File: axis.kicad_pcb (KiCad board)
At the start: 4 copper layers, 66 x 18 mm, 48 parts, among them J101 CORTEX-DEBUG, J102 JAE_DX07S016JA1R1500, SW101 SW_Push, SW102 SW_Push, U101 BHI160, U102 ATSAMD51G, U103 BMM150, U104 AP2112K-3.3, Y101 32.768kHz

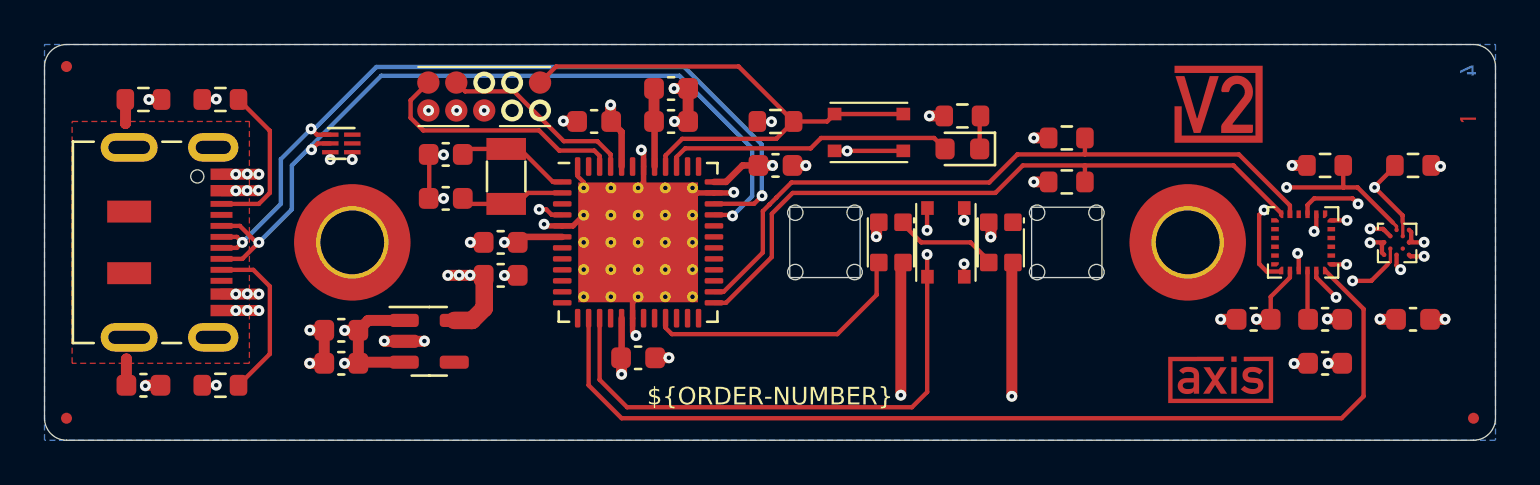
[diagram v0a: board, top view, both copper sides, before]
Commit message: Update to KiCat 7.0
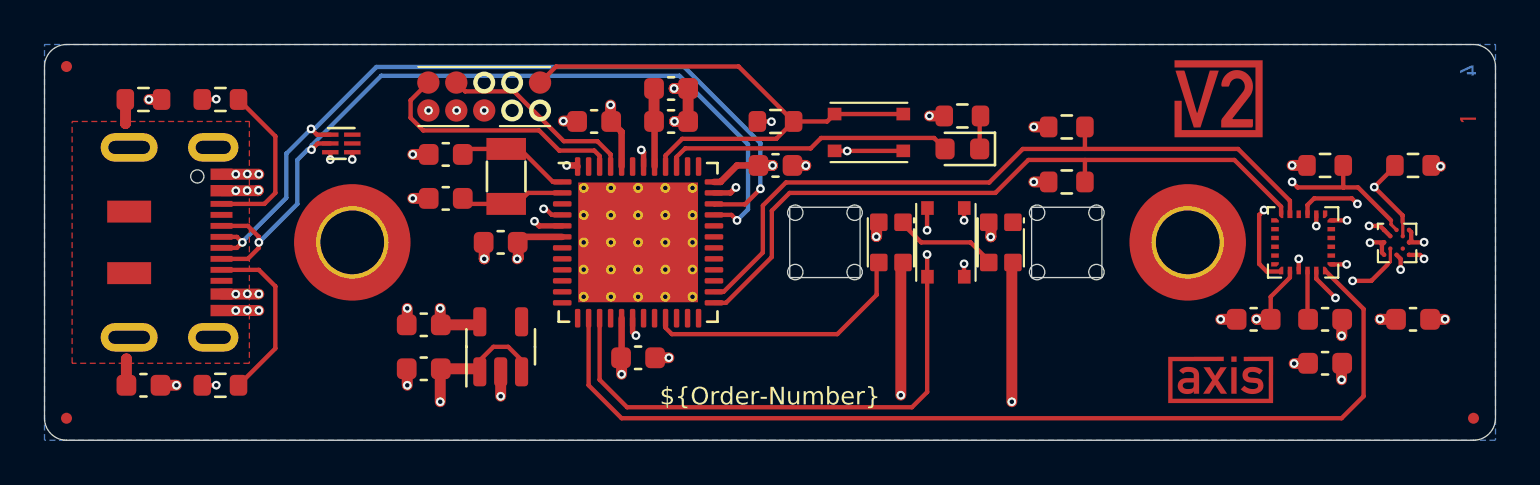
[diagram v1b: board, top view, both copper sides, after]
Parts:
- removed C115: 100n, Capacitor_SMD:C_0603_1608Metric
- C104, C105, C108, C109, C110, C111, C113, C116: value 100n -> 0u1
- C106: value 470n -> 0u47
- J102: value JAE_DX07S016JA1R1500 -> JAE_DX07S016JA3; footprint V2_Connector_USB:JAE_DX07S016JA1R1500 -> V2_Connector_USB:JAE_DX07S016JA3
- R101, R102, R104, R105: value 4k7 -> 5k1
- SPACER101, SPACER102: value 977?2434030 -> 9774030243
- Y101: value 32.768kHz -> 32k768
- moved C112 4.16 mm to (134.2, 109.8), turned to 180 degrees
- moved C114 3.76 mm to (134.2, 111.8)
- moved U104 3.26 mm to (137.8, 110.8), turned to 90 degrees
- moved R102 0.50 mm to (163.5, 100.8)
- moved ICON102 0.25 mm to (170.5, 99.5)
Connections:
- net +3.3V renamed +3V3
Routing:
- net GND: track 43.9 -> 34.8 mm, vias 46 -> 45
- net +3V3: track 27.3 -> 25.4 mm, vias 20 -> 18
- net /SCK: track 32.0 -> 32.8 mm
- net /SDA: track 31.2 -> 32.0 mm
- net /USB-: track 37.5 -> 38.1 mm
- net +5V: vias 11 -> 10

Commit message: Refresh
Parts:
- R101, R102, R104, R105: value 5k1 -> 2k7
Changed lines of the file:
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@@
         (effects (font (size 1 1) (thickness 0.15)))
     )
-    (fp_text value "5k1" (at 0 1.43) (layer "F.Fab") hide
+    (fp_text value "2k7" (at 0 1.43) (layer "F.Fab") hide
         (effects (font (size 1 1) (thickness 0.15)))
     )
@@
     (fp_line (start 3.5 3.5) (end -3.5 3.5)
       (stroke (width 0.1) (type solid)) (layer "F.Fab"))
-    (pad "" smd roundrect (at -1.85625 -1.85625) (size 1.098483 1.098483) (layers "F.Paste") (roundrect_rratio 0.227587))
-    (pad "" smd roundrect (at -1.85625 -0.61875) (size 1.098483 1.098483) (layers "F.Paste") (roundrect_rratio 0.227587))
-    (pad "" smd roundrect (at -1.85625 0.61875) (size 1.098483 1.098483) (layers "F.Paste") (roundrect_rratio 0.227587))
-    (pad "" smd roundrect (at -1.85625 1.85625) (size 1.098483 1.098483) (layers "F.Paste") (roundrect_rratio 0.227587))
-    (pad "" smd roundrect (at -0.61875 -1.85625) (size 1.098483 1.098483) (layers "F.Paste") (roundrect_rratio 0.227587))
-    (pad "" smd roundrect (at -0.61875 -0.61875) (size 1.098483 1.098483) (layers "F.Paste") (roundrect_rratio 0.227587))
-    (pad "" smd roundrect (at -0.61875 0.61875) (size 1.098483 1.098483) (layers "F.Paste") (roundrect_rratio 0.227587))
-    (pad "" smd roundrect (at -0.61875 1.85625) (size 1.098483 1.098483) (layers "F.Paste") (roundrect_rratio 0.227587))
-    (pad "" smd roundrect (at 0.61875 -1.85625) (size 1.098483 1.098483) (layers "F.Paste") (roundrect_rratio 0.227587))
-    (pad "" smd roundrect (at 0.61875 -0.61875) (size 1.098483 1.098483) (layers "F.Paste") (roundrect_rratio 0.227587))
-    (pad "" smd roundrect (at 0.61875 0.61875) (size 1.098483 1.098483) (layers "F.Paste") (roundrect_rratio 0.227587))
-    (pad "" smd roundrect (at 0.61875 1.85625) (size 1.098483 1.098483) (layers "F.Paste") (roundrect_rratio 0.227587))
-    (pad "" smd roundrect (at 1.85625 -1.85625) (size 1.098483 1.098483) (layers "F.Paste") (roundrect_rratio 0.227587))
-    (pad "" smd roundrect (at 1.85625 -0.61875) (size 1.098483 1.098483) (layers "F.Paste") (roundrect_rratio 0.227587))
-    (pad "" smd roundrect (at 1.85625 0.61875) (size 1.098483 1.098483) (layers "F.Paste") (roundrect_rratio 0.227587))
-    (pad "" smd roundrect (at 1.85625 1.85625) (size 1.098483 1.098483) (layers "F.Paste") (roundrect_rratio 0.227587))
+    (pad "" smd roundrect (at -1.85625 -1.85625) (size 0.95 0.95) (layers "F.Paste") (roundrect_rratio 0.1))
+    (pad "" smd roundrect (at -1.85625 -0.61875) (size 0.95 0.95) (layers "F.Paste") (roundrect_rratio 0.1))
+    (pad "" smd roundrect (at -1.85625 0.61875) (size 0.95 0.95) (layers "F.Paste") (roundrect_rratio 0.1))
+    (pad "" smd roundrect (at -1.85625 1.85625) (size 0.95 0.95) (layers "F.Paste") (roundrect_rratio 0.1))
+    (pad "" smd roundrect (at -0.61875 -1.85625) (size 0.95 0.95) (layers "F.Paste") (roundrect_rratio 0.1))
+    (pad "" smd roundrect (at -0.61875 -0.61875) (size 0.95 0.95) (layers "F.Paste") (roundrect_rratio 0.1))
+    (pad "" smd roundrect (at -0.61875 0.61875) (size 0.95 0.95) (layers "F.Paste") (roundrect_rratio 0.1))
+    (pad "" smd roundrect (at -0.61875 1.85625) (size 0.95 0.95) (layers "F.Paste") (roundrect_rratio 0.1))
+    (pad "" smd roundrect (at 0.61875 -1.85625) (size 0.95 0.95) (layers "F.Paste") (roundrect_rratio 0.1))
+    (pad "" smd roundrect (at 0.61875 -0.61875) (size 0.95 0.95) (layers "F.Paste") (roundrect_rratio 0.1))
+    (pad "" smd roundrect (at 0.61875 0.61875) (size 0.95 0.95) (layers "F.Paste") (roundrect_rratio 0.1))
+    (pad "" smd roundrect (at 0.61875 1.85625) (size 0.95 0.95) (layers "F.Paste") (roundrect_rratio 0.1))
+    (pad "" smd roundrect (at 1.85625 -1.85625) (size 0.95 0.95) (layers "F.Paste") (roundrect_rratio 0.1))
+    (pad "" smd roundrect (at 1.85625 -0.61875) (size 0.95 0.95) (layers "F.Paste") (roundrect_rratio 0.1))
+    (pad "" smd roundrect (at 1.85625 0.61875) (size 0.95 0.95) (layers "F.Paste") (roundrect_rratio 0.1))
+    (pad "" smd roundrect (at 1.85625 1.85625) (size 0.95 0.95) (layers "F.Paste") (roundrect_rratio 0.1))
     (pad "1" smd roundrect (at -3.45 -2.75) (size 0.85 0.25) (layers "F.Cu" "F.Paste" "F.Mask") (roundrect_rratio 0.25)
       (net 34 "/XIN32") (pinfunction "XIN32") (pintype "input"))
@@
         (effects (font (size 1 1) (thickness 0.15)))
     )
-    (fp_text value "5k1" (at 0 1.43) (layer "F.Fab") hide
+    (fp_text value "2k7" (at 0 1.43) (layer "F.Fab") hide
         (effects (font (size 1 1) (thickness 0.15)))
     )
@@
       )
     )
-    (group "" (id 358ee51b-4422-456b-95e9-9f0ef003cb42)
+    (group "" (id ddba60c9-c50d-451f-8487-0974804ab1e2)
       (members
-        0b67a753-43eb-4118-adb3-e29e86749380
-        1aa40552-c18a-49aa-a698-63ac6c12b314
-        34179935-ae31-405d-94ac-500255afee93
-        759a353d-041c-4219-93d1-40e8314815a5
-        ee6be92e-1a1c-400f-a09f-b98af1d75dad
-        fc1a7954-e7f7-44e6-a2b9-d8ee128978e3
+        224847d1-2864-415e-8443-57ea01c235d4
+        24ac9303-677a-4214-aa0a-fcecac6cdac4
+        61703b29-828f-4601-9bcf-6587c7e49d2b
+        6c2760c4-e44c-48f5-8ad6-c06ba8209fa3
+        8149f5a1-a6c9-4ba1-a14a-457c718db283
+        dc3a6b00-39ae-45d0-924f-0a7a0821cd1a
       )
     )
-    (group "" (id e0c8cf57-0d2c-47fd-bb76-ad2c0bf2787a)
+    (group "" (id c475bc90-ff89-4c5c-ba69-515d1fe08198)
       (members
-        03b82d5e-cbeb-469d-8d84-997bcf50f3e0
-        5d32b6cb-796b-410a-961c-27a04f76b46e
-        d2dd2408-0506-472f-8d14-85ca5f8b1289
-        d7e241cc-6909-4050-bd80-9787c5134abf
-        d89baf6d-6b75-4805-ad61-920d0022b002
-        e30e904e-965a-4282-93a2-345aced02028
+        046ed7af-14b4-4c5c-a8d6-1b2eb7cb106d
+        2b9fbc84-d749-46a9-82bb-40c9dba44955
+        5b896870-6cc5-441a-9a4b-ca42b4f9f712
+        90415b5e-18c0-4554-8cf6-056854a1a20f
+        af8c352d-318f-494e-8294-8604418917e4
+        eaaa4020-0c8f-4240-9fab-425fb90bc987
       )
     )
@@
         (effects (font (size 1 1) (thickness 0.15)))
     )
-    (fp_text value "5k1" (at 0 1.43) (layer "F.Fab") hide
+    (fp_text value "2k7" (at 0 1.43) (layer "F.Fab") hide
         (effects (font (size 1 1) (thickness 0.15)))
     )
@@
         (effects (font (size 1 1) (thickness 0.15)))
     )
-    (fp_text value "5k1" (at 0 1.43) (layer "F.Fab") hide
+    (fp_text value "2k7" (at 0 1.43) (layer "F.Fab") hide
         (effects (font (size 1 1) (thickness 0.15)))
     )
